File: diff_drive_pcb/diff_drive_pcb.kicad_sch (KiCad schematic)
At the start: 17 parts, among them J1 P_M1, J10 12V_IN, J11 Motor_Break_SW, J12 POWER_SW, J2 Encoder_M1, J3 P_M2, J4 Encoder_M2, J5 P_M3, J6 Encoder_M3, J7 P_M4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

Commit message: Isolated 12V GND from uC GND
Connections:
- net GND: no longer J10.2 (Pin_2)
- new net GND1: J10.2 (Pin_2), U1.12 (PGND), U2.12 (PGND)
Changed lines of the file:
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@@
 	(wire
 		(pts
+			(xy 67.31 57.15) (xy 55.88 57.15)
+		)
+		(stroke
+			(width 0)
+			(type default)
+		)
+	)
+	(wire
+		(pts
 			(xy 31.75 55.88) (xy 31.75 54.61)
 		)
@@
 	(wire
 		(pts
-			(xy 127 55.88) (xy 120.65 55.88)
+			(xy 127 54.61) (xy 120.65 54.61)
 		)
 		(stroke
@@
 	(wire
 		(pts
+			(xy 132.08 57.15) (xy 120.65 57.15)
+		)
+		(stroke
+			(width 0)
+			(type default)
+		)
+	)
+	(wire
+		(pts
 			(xy 266.7 71.12) (xy 266.7 73.66)
 		)
@@
 	(wire
 		(pts
+			(xy 67.31 66.04) (xy 67.31 57.15)
+		)
+		(stroke
+			(width 0)
+			(type default)
+		)
+	)
+	(wire
+		(pts
 			(xy 73.66 156.21) (xy 80.01 156.21)
 		)
@@
 	(wire
 		(pts
-			(xy 62.23 55.88) (xy 55.88 55.88)
+			(xy 62.23 54.61) (xy 55.88 54.61)
 		)
 		(stroke
@@
 	(wire
 		(pts
+			(xy 132.08 69.85) (xy 132.08 57.15)
+		)
+		(stroke
+			(width 0)
+			(type default)
+		)
+	)
+	(wire
+		(pts
 			(xy 96.52 54.61) (xy 99.06 54.61)
 		)
@@
 		(pin "3"
 		)
+		(pin "12"
+		)
 		(instances
 			(project "diff_drive_pcb"
@@
 	)
 	(symbol
+		(lib_name "MDD3A_1")
 		(lib_id "MDD3A:MDD3A")
 		(at 44.45 54.61 0)
@@
 		(pin "3"
 		)
+		(pin "12"
+		)
 		(instances
 			(project ""
@@
 	(symbol
 		(lib_id "power:+12V")
-		(at 127 55.88 270)
+		(at 127 54.61 270)
 		(unit 1)
 		(exclude_from_sim no)
@@
 		(fields_autoplaced yes)
 		(property "Reference" "#PWR09"
-			(at 123.19 55.88 0)
+			(at 123.19 54.61 0)
 			(effects
 				(font
@@
 		)
 		(property "Value" "+12V"
-			(at 130.81 55.8799 90)
+			(at 130.81 54.6099 90)
 			(effects
 				(font
@@
 		)
 		(property "Footprint" ""
-			(at 127 55.88 0)
+			(at 127 54.61 0)
 			(effects
 				(font
@@
 		)
 		(property "Datasheet" ""
-			(at 127 55.88 0)
+			(at 127 54.61 0)
 			(effects
 				(font
@@
 		)
 		(property "Description" "Power symbol creates a global label with name \"+12V\""
-			(at 127 55.88 0)
+			(at 127 54.61 0)
 			(effects
 				(font
@@
 	)
 	(symbol
+		(lib_id "power:GND1")
+		(at 115.57 114.3 0)
+		(unit 1)
+		(exclude_from_sim no)
+		(in_bom yes)
+		(on_board yes)
+		(dnp no)
+		(fields_autoplaced yes)
+		(property "Reference" "#PWR013"
+			(at 115.57 120.65 0)
+			(effects
+				(font
+					(size 1.27 1.27)
+				)
+				(hide yes)
+			)
+		)
+		(property "Value" "GND1"
+			(at 115.57 119.38 0)
+			(effects
+				(font
+					(size 1.27 1.27)
+				)
+			)
+		)
+		(property "Footprint" ""
+			(at 115.57 114.3 0)
+			(effects
+				(font
+					(size 1.27 1.27)
+				)
+				(hide yes)
+			)
+		)
+		(property "Datasheet" ""
+			(at 115.57 114.3 0)
+			(effects
+				(font
+					(size 1.27 1.27)
+				)
+				(hide yes)
+			)
+		)
+		(property "Description" "Power symbol creates a global label with name \"GND1\" , ground"
+			(at 115.57 114.3 0)
+			(effects
+				(font
+					(size 1.27 1.27)
+				)
+				(hide yes)
+			)
+		)
+		(pin "1"
+		)
+		(instances
+			(project ""
+				(path "/1d6015c4-e67e-4a12-847c-bf56cfcabd56"
+					(reference "#PWR013")
+					(unit 1)
+				)
+			)
+		)
+	)
+	(symbol
 		(lib_id "Device:Buzzer")
 		(at 40.64 177.8 0)
@@
 	)
 	(symbol
+		(lib_id "power:GND1")
+		(at 132.08 69.85 0)
+		(unit 1)
+		(exclude_from_sim no)
+		(in_bom yes)
+		(on_board yes)
+		(dnp no)
+		(fields_autoplaced yes)
+		(property "Reference" "#PWR023"
+			(at 132.08 76.2 0)
+			(effects
+				(font
+					(size 1.27 1.27)
+				)
+				(hide yes)
+			)
+		)
+		(property "Value" "GND1"
+			(at 132.08 74.93 0)
+			(effects
+				(font
+					(size 1.27 1.27)
+				)
+			)
+		)
+		(property "Footprint" ""
+			(at 132.08 69.85 0)
+			(effects
+				(font
+					(size 1.27 1.27)
+				)
+				(hide yes)
+			)
+		)
+		(property "Datasheet" ""
+			(at 132.08 69.85 0)
+			(effects
+				(font
+					(size 1.27 1.27)
+				)
+				(hide yes)
+			)
+		)
+		(property "Description" "Power symbol creates a global label with name \"GND1\" , ground"
+			(at 132.08 69.85 0)
+			(effects
+				(font
+					(size 1.27 1.27)
+				)
+				(hide yes)
+			)
+		)
+		(pin "1"
+		)
+		(instances
+			(project "diff_drive_pcb"
+				(path "/1d6015c4-e67e-4a12-847c-bf56cfcabd56"
+					(reference "#PWR023")
+					(unit 1)
+				)
+			)
+		)
+	)
+	(symbol
 		(lib_id "power:+5V")
 		(at 110.49 154.94 270)
@@
 	)
 	(symbol
+		(lib_id "power:GND1")
+		(at 67.31 66.04 0)
+		(unit 1)
+		(exclude_from_sim no)
+		(in_bom yes)
+		(on_board yes)
+		(dnp no)
+		(fields_autoplaced yes)
+		(property "Reference" "#PWR015"
+			(at 67.31 72.39 0)
+			(effects
+				(font
+					(size 1.27 1.27)
+				)
+				(hide yes)
+			)
+		)
+		(property "Value" "GND1"
+			(at 67.31 71.12 0)
+			(effects
+				(font
+					(size 1.27 1.27)
+				)
+			)
+		)
+		(property "Footprint" ""
+			(at 67.31 66.04 0)
+			(effects
+				(font
+					(size 1.27 1.27)
+				)
+				(hide yes)
+			)
+		)
+		(property "Datasheet" ""
+			(at 67.31 66.04 0)
+			(effects
+				(font
+					(size 1.27 1.27)
+				)
+				(hide yes)
+			)
+		)
+		(property "Description" "Power symbol creates a global label with name \"GND1\" , ground"
+			(at 67.31 66.04 0)
+			(effects
+				(font
+					(size 1.27 1.27)
+				)
+				(hide yes)
+			)
+		)
+		(pin "1"
+		)
+		(instances
+			(project "diff_drive_pcb"
+				(path "/1d6015c4-e67e-4a12-847c-bf56cfcabd56"
+					(reference "#PWR015")
+					(unit 1)
+				)
+			)
+		)
+	)
+	(symbol
 		(lib_id "Connector:Conn_01x02_Pin")
 		(at 104.14 97.79 0)
@@
 	(symbol
 		(lib_id "power:+12V")
-		(at 62.23 55.88 270)
+		(at 62.23 54.61 270)
 		(unit 1)
 		(exclude_from_sim no)
@@
 		(fields_autoplaced yes)
 		(property "Reference" "#PWR039"
-			(at 58.42 55.88 0)
+			(at 58.42 54.61 0)
 			(effects
 				(font
@@
 		)
 		(property "Value" "+12V"
-			(at 66.04 55.8799 90)
+			(at 66.04 54.6099 90)
 			(effects
 				(font
@@
 		)
 		(property "Footprint" ""
-			(at 62.23 55.88 0)
+			(at 62.23 54.61 0)
 			(effects
 				(font
@@
 		)
 		(property "Datasheet" ""
-			(at 62.23 55.88 0)
+			(at 62.23 54.61 0)
 			(effects
 				(font
@@
 		)
 		(property "Description" "Power symbol creates a global label with name \"+12V\""
-			(at 62.23 55.88 0)
+			(at 62.23 54.61 0)
 			(effects
 				(font
@@
 					(unit 1)
 				)
-			)
-		)
-	)
-	(symbol
-		(lib_id "power:GND")
-		(at 115.57 114.3 0)
-		(unit 1)
-		(exclude_from_sim no)
-		(in_bom yes)
-		(on_board yes)
-		(dnp no)
-		(fields_autoplaced yes)
-		(property "Reference" "#PWR015"
-			(at 115.57 120.65 0)
-			(effects
-				(font
-					(size 1.27 1.27)
-				)
-				(hide yes)
-			)
-		)
-		(property "Value" "GND"
-			(at 115.57 119.38 0)
-			(effects
-				(font
-					(size 1.27 1.27)
-				)
-			)
-		)
-		(property "Footprint" ""
-			(at 115.57 114.3 0)
-			(effects
-				(font
-					(size 1.27 1.27)
-				)
-				(hide yes)
-			)
-		)
-		(property "Datasheet" ""
-			(at 115.57 114.3 0)
-			(effects
-				(font
-					(size 1.27 1.27)
-				)
-				(hide yes)
-			)
-		)
-		(property "Description" "Power symbol creates a global label with name \"GND\" , ground"
-			(at 115.57 114.3 0)
-			(effects
-				(font
-					(size 1.27 1.27)
-				)
-				(hide yes)
-			)
-		)
-		(pin "1"
-		)
-		(instances
-			(project "diff_drive_pcb"
-				(path "/1d6015c4-e67e-4a12-847c-bf56cfcabd56"
-					(reference "#PWR015")
-					(unit 1)
-				)

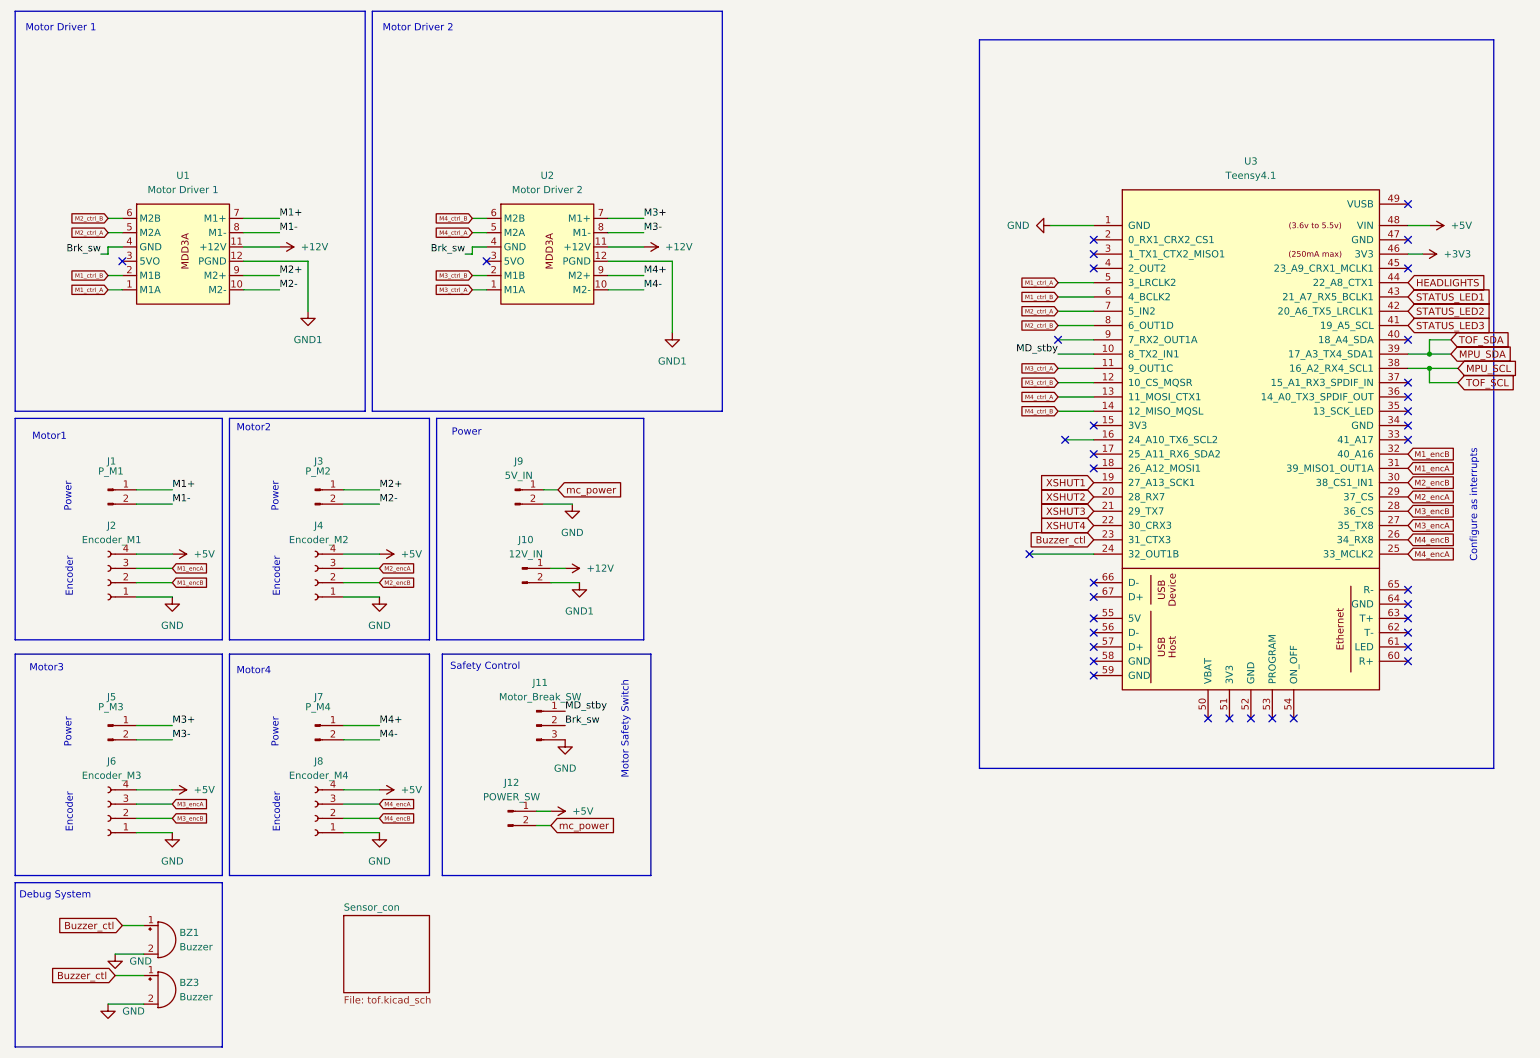
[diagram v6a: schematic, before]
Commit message: V2.2 changes to power system
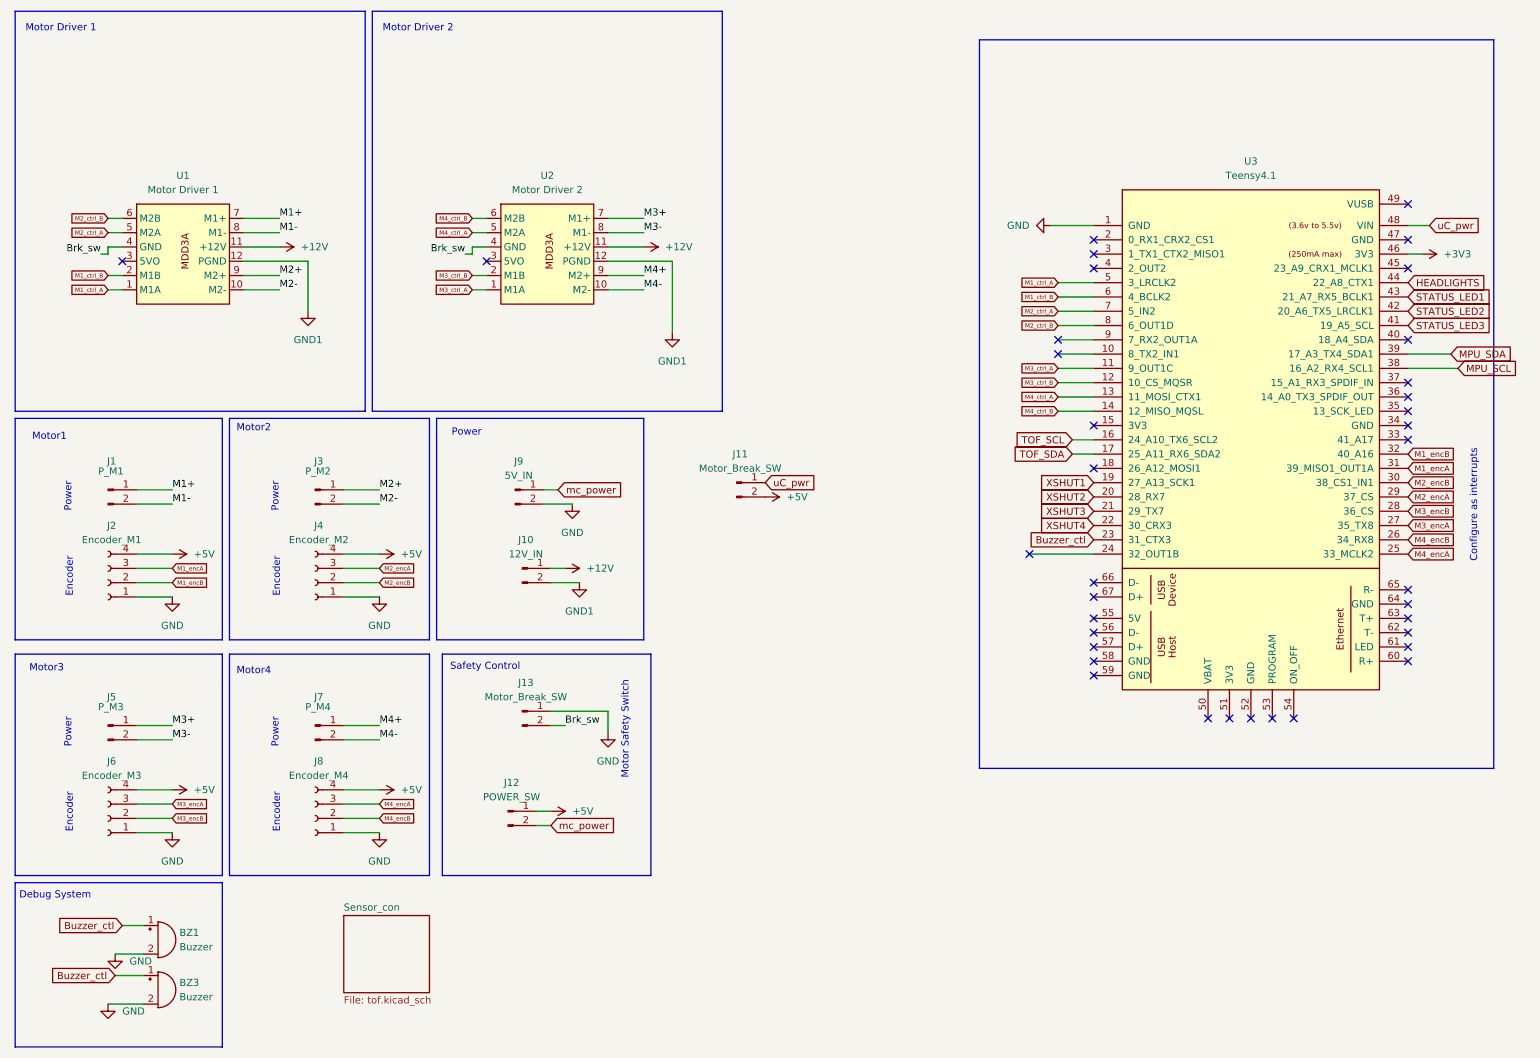
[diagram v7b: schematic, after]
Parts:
- removed J11: Motor_Break_SW, Connector_PinHeader_2.54mm:PinHeader_1x03_P2.54mm_Vertical, symbol Connector:Conn_01x03_Pin
- added J11, J13: Motor_Break_SW, Connector_PinHeader_2.54mm:PinHeader_1x02_P2.54mm_Vertical, symbol Connector:Conn_01x02_Pin
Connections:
- net +5V: now also J11.2 (Pin_2); no longer U3.48 (VIN)
- net Brk_sw: now also J13.2 (Pin_2)
- net GND: now also J13.1 (Pin_1)
- net TOF_SCL: now reaches U3.16 (24_A10_TX6_SCL2)
- net TOF_SDA: now reaches U3.17 (25_A11_RX6_SDA2)
- net MD_stby: no longer names the net of U3.10 (8_TX2_IN1)
- new net uC_pwr: J11.1 (Pin_1), U3.48 (VIN)
- no-connect marks 38 -> 37
